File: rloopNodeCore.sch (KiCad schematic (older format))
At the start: 20 parts

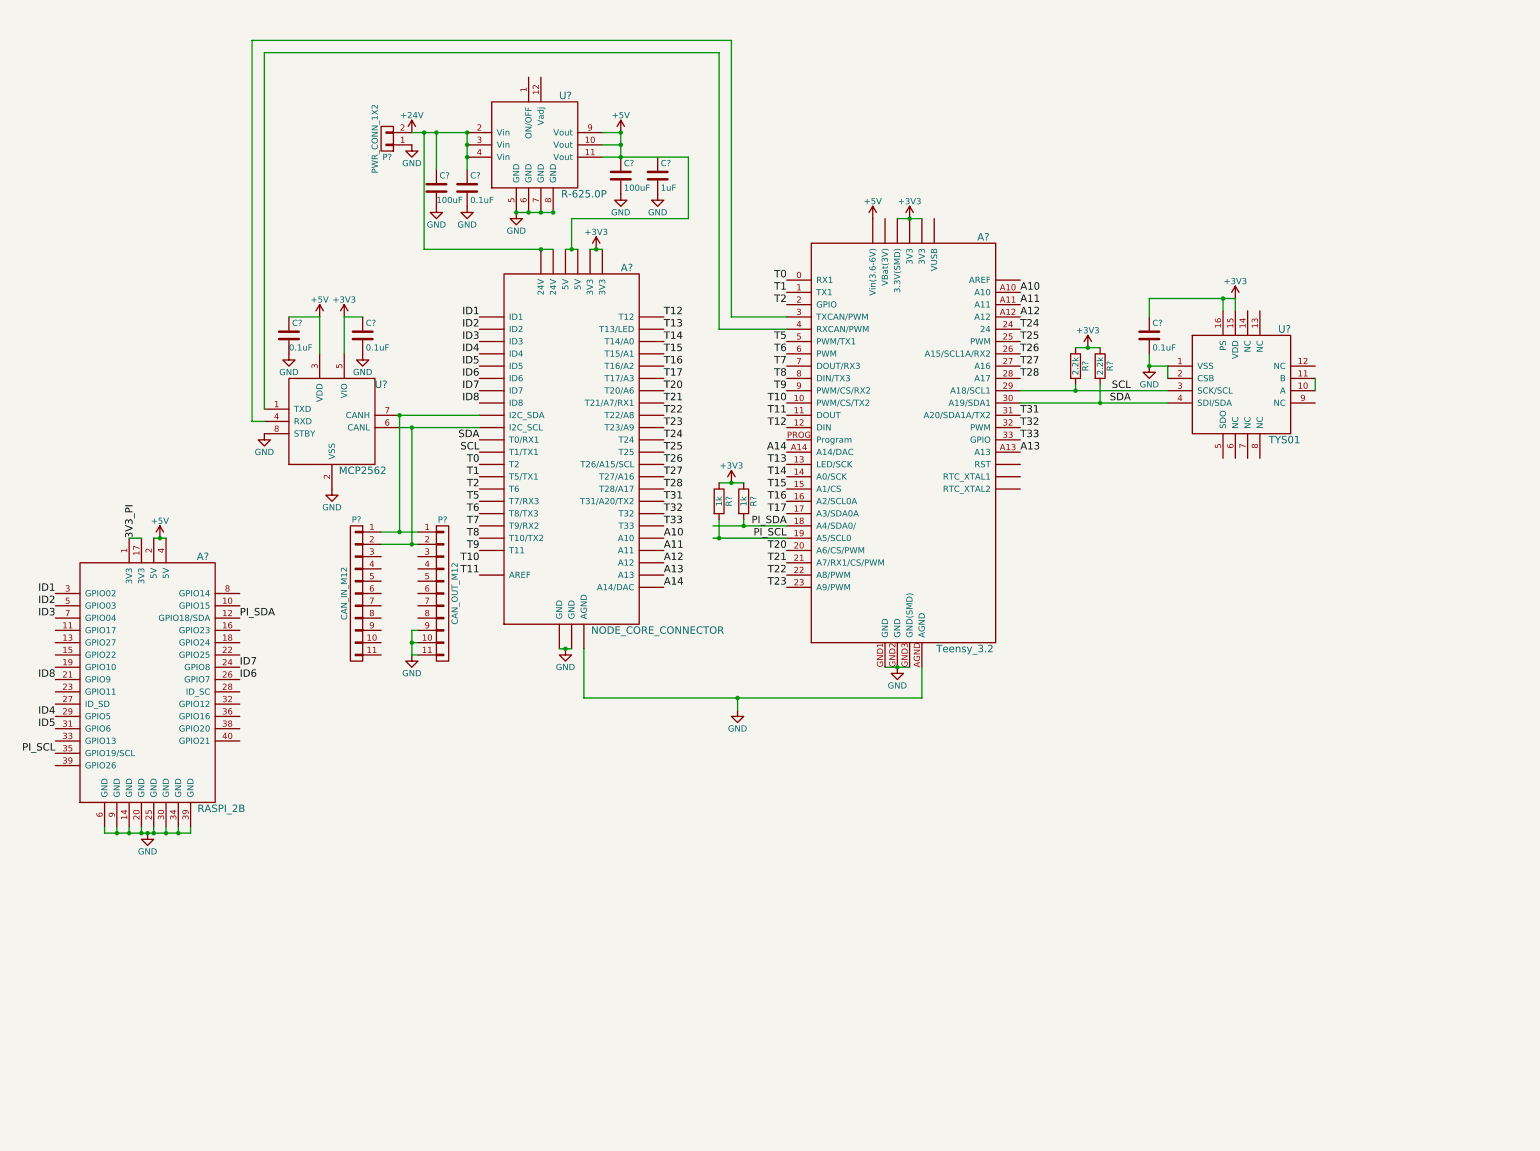
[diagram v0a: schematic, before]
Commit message: v0.2
Added I2C isolator
Added 24V input diode
Added power rail test points and indicator LEDs
More power supply filter caps
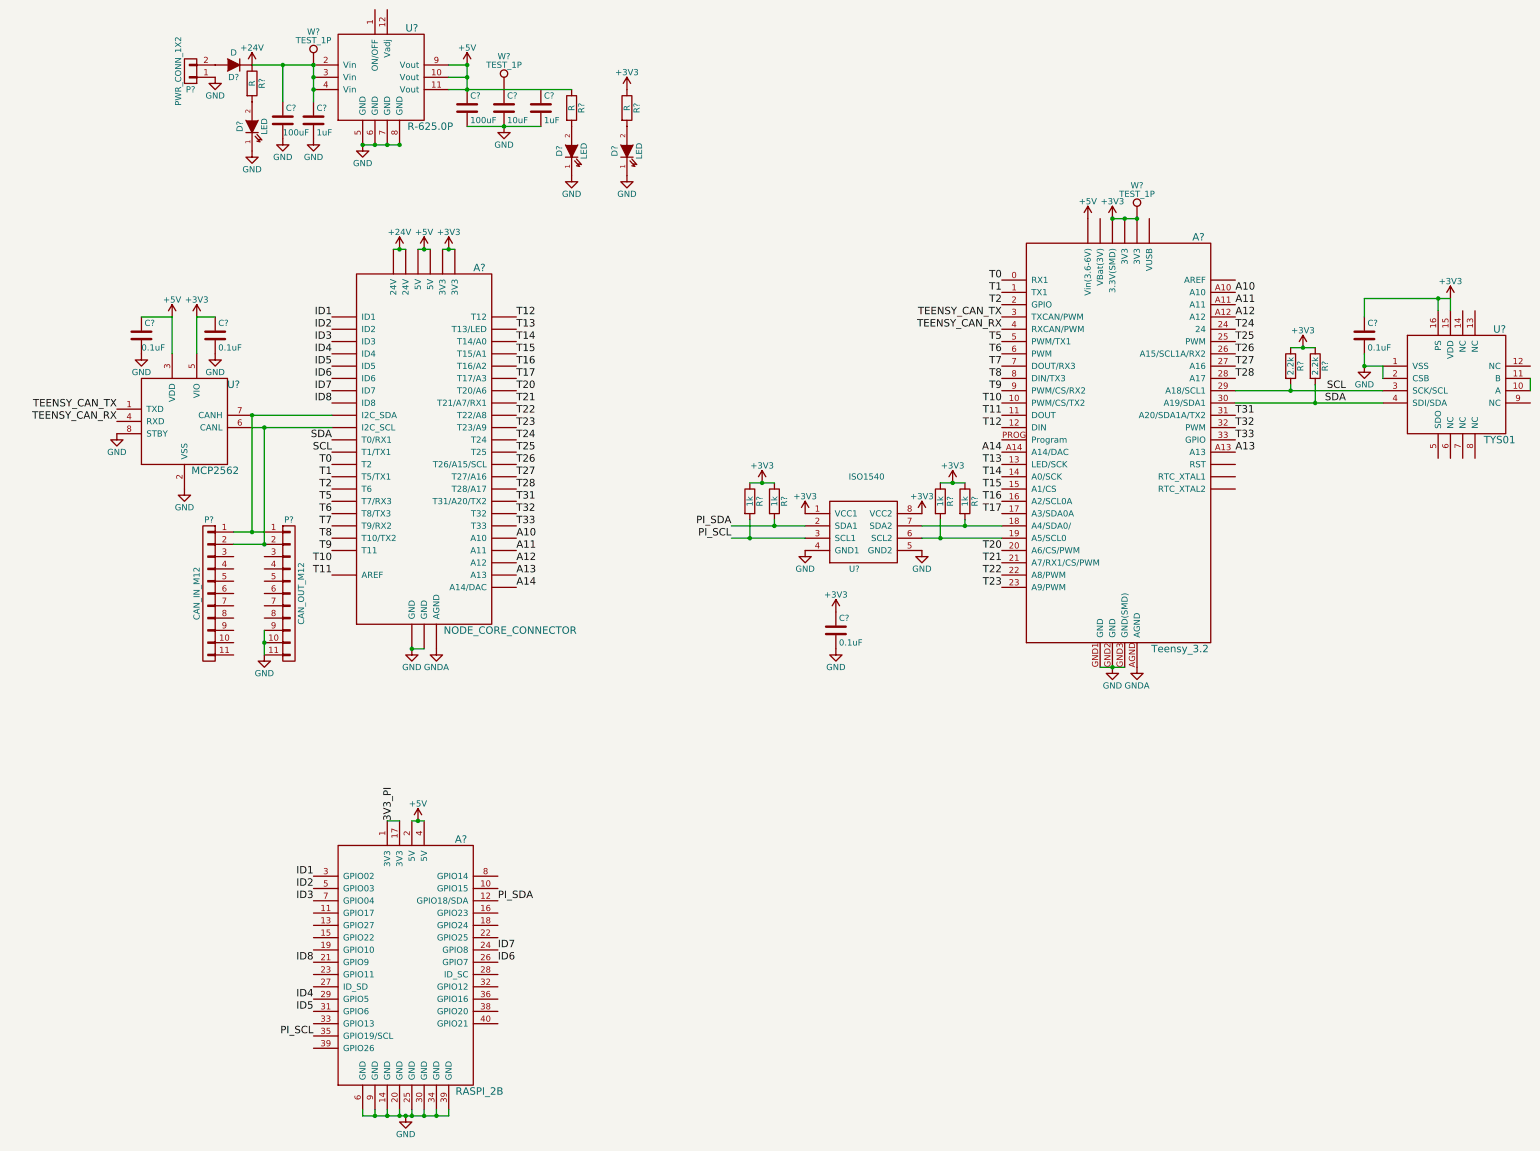
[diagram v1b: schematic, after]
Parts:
- added C?: 0.1uF, symbol C
- added C?: 1uF, symbol C
- added D?: D, symbol D
- added D? (x3): LED, symbol LED
- added R? (x3): R, symbol R
- added R? (x2): 1k, symbol R
- added U?: ISO1540, symbol ISO1540
- added W? (x3): TEST_1P, symbol TEST_1P
- C?: value 0.1uF -> 1uF
- C?: value 1uF -> 10uF
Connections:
- net +24V: now also D?.1 (K), R?.1, W?.1; no longer P?.2 (P2)
- net +3V3: now also C?.1, R?.1, R?.1, R?.1, U?.1 (VCC1), U?.8 (VCC2), W?.1
- net +5V: now also R?.1
- net GND: now also C?.2, C?.2, D?.1 (K), D?.1 (K), D?.1 (K), U?.4 (GND1), U?.5 (GND2); no longer A?.AGND, A?.AGND
- net PI_SCL: now also R?.2, U?.3 (SCL1); no longer A?.19 (A5/SCL0), R?.2
- net PI_SDA: now also R?.2, U?.2 (SDA1); no longer A?.18 (A4/SDA0/), R?.2
- net TEENSY_CAN_RX: now reaches U?.4 (RXD)
- net TEENSY_CAN_RX: now also A?.4 (RXCAN/PWM); no longer A?.3 (TXCAN/PWM)
- net TEENSY_CAN_TX: now reaches U?.1 (TXD)
- net TEENSY_CAN_TX: now also A?.3 (TXCAN/PWM); no longer A?.4 (RXCAN/PWM)
- net at C?.1: now also W?.1
- new net: A?.18 (A4/SDA0/), R?.2, U?.7 (SDA2)
- new net: A?.19 (A5/SCL0), R?.2, U?.6 (SCL2)
- new net: D?.2 (A), P?.2 (P2)
- new net: D?.2 (A), R?.2 (x3)
- new net GNDA: A?.AGND, A?.AGND
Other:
- moved on the sheet: A?, C?, P?, R?, U?

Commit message: v0.3
Added optional ferrite choke between GND and AGND
Isolated I2C transceiver supply voltages
Removed CAN from Node Core Connector
Added program pin jumper
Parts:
- added C?: 0.1uF, symbol C
- added JP?: Jumper_NO_Small, symbol Jumper_NO_Small
- added L?: FERRITE_INDUCTOR, symbol INDUCTOR_SMALL
- added R? (x8): 10K, symbol R
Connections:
- net +3V3: no longer R?.1, R?.1, U?.1 (VCC1)
- net 3V3_PI: now also R?.1, R?.1, U?.1 (VCC1), C?.1, R?.2, R?.2, R?.2, R?.2, R?.2, R?.2, R?.2, R?.2
- net GND: now also C?.2, L?.1
- net GNDA: now also L?.2
- net ID1: now also R?.1
- net ID2: now also R?.1
- net ID3: now also R?.1
- net ID4: now also R?.1
- net ID5: now also R?.1
- net ID6: now also R?.1
- net ID7: now also R?.1
- net ID8: now also R?.1
- net SCL: now also A?.T29 (I2C_SCL); no longer A?.T1 (T1/TX1)
- net SDA: now also A?.T30 (I2C_SDA); no longer A?.T0 (T0/RX1)
- net T0: now also A?.T0 (T0/RX1); no longer A?.T2
- net T1: now also A?.T1 (T1/TX1); no longer A?.T5 (T5/TX1)
- net T10: now also A?.T10 (T10/TX2)
- net T11: now also A?.T11; no longer A?.AREF
- net T2: now also A?.T2; no longer A?.T6
- net T5: now also A?.T5 (T5/TX1); no longer A?.T7 (T7/RX3)
- net T6: now also A?.T6; no longer A?.T8 (T8/TX3)
- net T7: now also A?.T7 (T7/RX3); no longer A?.T9 (T9/RX2)
- net T8: now also A?.T8 (T8/TX3); no longer A?.T10 (T10/TX2)
- net T9: now also A?.T9 (T9/RX2); no longer A?.T11
- net PROG: now reaches A?.19 (GPIO10)
- net PROG: now also JP?.1
- net at A?.PROG (Program): now also JP?.2
- net at P?.2 (P2), P?.2 (P2), U?.6 (CANL): no longer A?.T29 (I2C_SCL)
- net at P?.1 (P1), P?.1 (P1), U?.7 (CANH): no longer A?.T30 (I2C_SDA)
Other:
- note added: "Ambient temperature sensor"
- note added: "Cable shield\ngrounded on one end"
- note added: "Pads for a higher current ferrite choke\nin case the Teensy's isn't good enough."
- note added: "Programming jumper for degugging\nRemove for operation"
- moved on the sheet: C?, P?, U?

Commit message: Formatting Improvements
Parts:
- added R?: 120, symbol R
- C? (x5): value 0.1uF -> 100nF
- R? (x2): value 2.2k -> 2K2
- R? (x2): value 1k -> 1K
- R? (x3): value R -> 1K2
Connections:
- net +3V3 is gone; now on net +24V: A?.+3V3 (3V3), A?.+3V3 (3V3), C?.1, C?.1, C?.1, R?.1, R?.1, R?.1, R?.1, R?.1, U?.15 (VDD), U?.16 (PS), U?.5 (VIO), U?.8 (VCC2), W?.1
- net +5V is gone; now on net +24V: A?.+5V (5V), A?.2 (5V), A?.4 (5V), A?.VIN (Vin(3.6-6V)), C?.1, C?.1, R?.1, U?.10 (Vout), U?.11 (Vout), U?.3 (VDD), U?.9 (Vout)
- net +24V: now also C?.1, C?.1, W?.1
- net at P?.1 (P1), P?.1 (P1), U?.7 (CANH): now also R?.1, R?.2
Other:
- note added: "24V In and 5V Supply"
- note added: "CAN Interface"
- note added: "Connector to rest of node"
- note added: "Normally unpopulated\ntermination resistor"
- note added: "Raspberry Pi 2B"
- note added: "Teensy Microcontroller\n"
- moved on the sheet: A?, C?, D?, JP?, L?, P?, R?, U?, W?

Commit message: 5/09
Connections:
- net +24V: no longer A?.+3V3 (3V3), A?.+3V3 (3V3), A?.+5V (5V), A?.2 (5V), A?.4 (5V), A?.VIN (Vin(3.6-6V)), C?.1, C?.1, C?.1, C?.1, C?.1, C?.1, C?.1, R?.1, R?.1, R?.1, R?.1, R?.1, R?.1, U?.10 (Vout), U?.11 (Vout), U?.15 (VDD), U?.16 (PS), U?.3 (VDD), U?.5 (VIO), U?.8 (VCC2), U?.9 (Vout), W?.1, W?.1
- net at P?.2 (P2), P?.2 (P2), U?.6 (CANL): now also R?.2
- net at P?.1 (P1), P?.1 (P1), R?.1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: no longer R?.2
- net +3V3: now reaches A?.+3V3 (3V3)
- net +3V3: now also A?.+3V3 (3V3), C?.1, C?.1, C?.1, R?.1, R?.1, R?.1, R?.1, R?.1, U?.15 (VDD), U?.16 (PS), U?.5 (VIO), U?.8 (VCC2), W?.1
- new net +5V: A?.+5V (5V), A?.2 (5V), A?.4 (5V), A?.VIN (Vin(3.6-6V)), C?.1, C?.1, C?.1, C?.1, R?.1, U?.10 (Vout), U?.11 (Vout), U?.3 (VDD), U?.9 (Vout), W?.1
- no-connect marks 0 -> 23
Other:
- moved on the sheet: C?, R?, U?

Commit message: just seeing how big everything is
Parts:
- A1: renamed from A?; footprint (none) -> -footprints:NODE-CORE
- A2: renamed from A?; footprint (none) -> -footprints:TEENSY-3.2
- A3: renamed from A?; footprint (none) -> Pin_Headers:Pin_Header_Straight_2x20
- C1, C4: renamed from C?; footprint (none) -> Capacitors_SMD:C_2225
- C10, C3, C6, C7, C8, C9: renamed from C?; footprint (none) -> Capacitors_SMD:C_0603
- C2: renamed from C?; footprint (none) -> Capacitors_SMD:C_1210
- C5: renamed from C?; footprint (none) -> Capacitors_SMD:C_1206
- D1: renamed from D?; footprint (none) -> Diodes_SMD:SMC_Standard
- D2, D3, D4: renamed from D?; footprint (none) -> LEDs:LED_0603
- JP1: renamed from JP?; footprint (none) -> Pin_Headers:Pin_Header_Straight_1x02
- L1: renamed from L?; footprint (none) -> Inductors:NR4018_HandSoldering
- P1: renamed from P?; footprint (none) -> -footprints:CONN-TE-MICROMNL-2-PTH-MALE-RGT; symbol CONN_01X02 -> CONN_01X02_2XMNT
- P2, P3: renamed from P?; footprint (none) -> -footprints:M12-TE-5-2172077-2; symbol CONN_01X11 -> CONN_01X08_2MNT
- R1, R11, R12, R13, R14, R15, R16, R17, R18, R2, R3, R4, R5, R6, R7, R8, R9: renamed from R?; footprint (none) -> Resistors_SMD:R_0603
- R10: renamed from R?; footprint (none) -> Resistors_SMD:R_1206_HandSoldering
- U1: renamed from U?; footprint (none) -> -footprints:R-6xxxP
- U2: renamed from U?; footprint (none) -> Housings_DFN_QFN:QFN-16-1EP_4x4mm_Pitch0.65mm
- U3, U4: renamed from U?; footprint (none) -> Housings_SOIC:SOIC-8_3.9x4.9mm_Pitch1.27mm
- W1, W2, W3: renamed from W?; footprint (none) -> Pin_Headers:Pin_Header_Straight_1x01
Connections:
- net GND: now also P3.M1, P3.M2; no longer P3.10 (P10), P3.11 (P11), P3.9 (P9)

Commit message: node core is almost done, awaiting review
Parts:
- added C2, C3: 100uF, Capacitors_SMD:c_elec_6.3x5.8, symbol CP1
- added D2: D, Diodes_SMD:SMC_Standard, symbol D
- added F1, F2: FUSE, -footprints:FUSEHOLDER-BLADE-LITTELFUSE-153, symbol FUSE
- added P2: PWR_CONN_1X2, -footprints:CONN-TE-MICROMNL-2-PTH-MALE-RGT, symbol CONN_01X02_2XMNT
- A1: footprint -footprints:NODE-CORE -> -footprints:NODECORE
- C1: renamed from C4; footprint Capacitors_SMD:C_2225 -> Capacitors_SMD:c_elec_6.3x5.8; symbol C -> CP1
- C5: renamed from C1; footprint Capacitors_SMD:C_2225 -> Capacitors_SMD:c_elec_6.3x5.8; symbol C -> CP1
- C6: renamed from C2; footprint Capacitors_SMD:C_1210 -> Capacitors_SMD:C_1206_HandSoldering; symbol C -> CP1
- renumbered A3 to A2, A2 to A3, C8 to C10, C10 to C11, C6 to C12, C5 to C4, C3 to C7, C9 to C8, C7 to C9, D2 to D3, D3 to D4, D4 to D5, P2 to P3, P3 to P4, R2 to R10, R3 to R11, R6 to R12, R7 to R13, R8 to R14, R9 to R15, R10 to R16, R4 to R17, R5 to R18, R11 to R2, R12 to R3, R13 to R4, R15 to R5, R17 to R6, R18 to R7, R14 to R8, R16 to R9, U4 to U2, U2 to U4, W3 to W2, W2 to W3
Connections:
- net +24V: now also C2.1, C3.1, D2.1 (K)
- net GND: now also P1.M1, P1.M2, P3.M1, P3.M2, C2.2, C3.2, P2.1 (P1), P2.M1, P2.M2
- net AREF: now reaches A3.AREF
- net AREF: now also A1.AREF
- net at P1.2 (P2): now also F1.1; no longer D1.2 (A)
- new net: D1.2 (A), F1.2
- new net: F2.1, P2.2 (P2)
- new net: D2.2 (A), F2.2
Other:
- moved on the sheet: A3, C10, C11, C12, C4, C7, C8, C9, D1, D4, D5, JP1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
